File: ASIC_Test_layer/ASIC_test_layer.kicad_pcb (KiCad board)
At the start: 4 copper layers, 37.5 x 30.4 mm, 20 parts, among them J100 MOLEX-524653071, J200 MOLEX-533073071, J5 5024262030, J6 MOLEX-533073071, J7 MOLEX-524653071, P11 Header 11X2, P12 Header 11X2, P13 Header 11X2

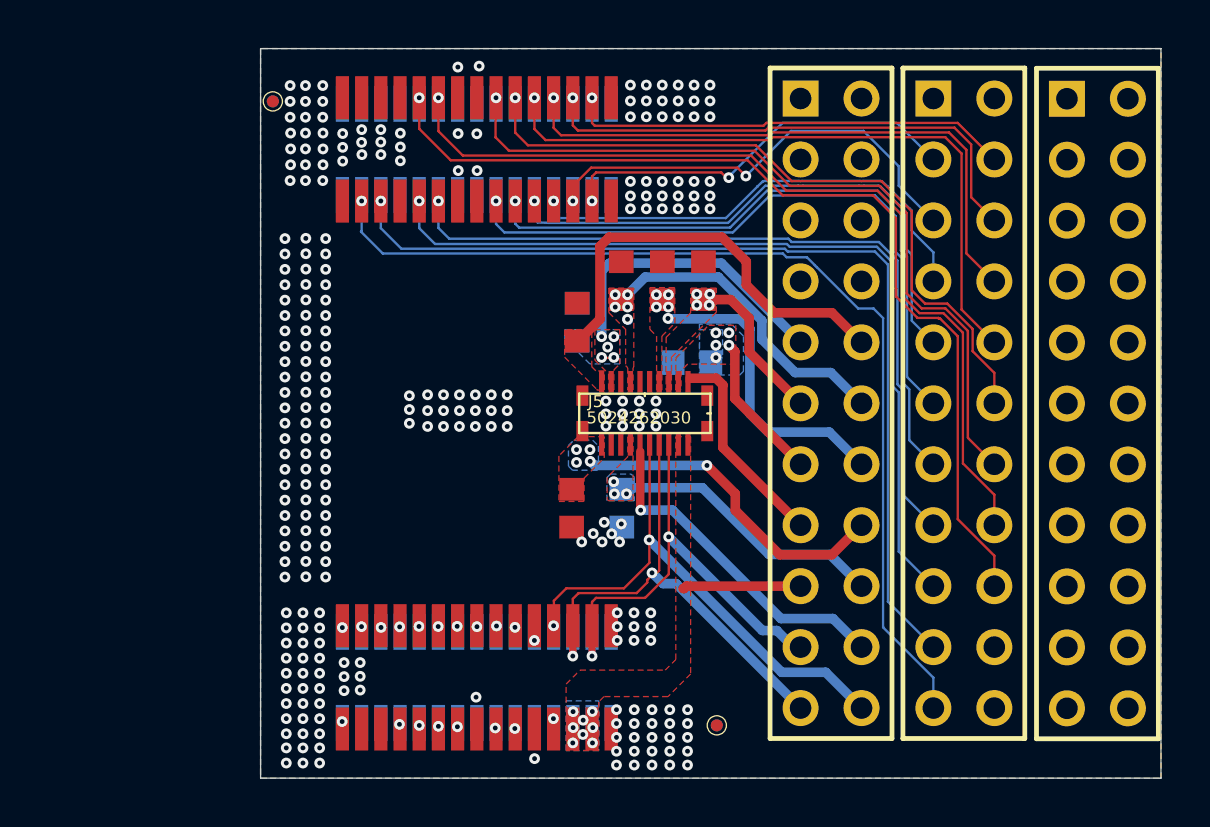
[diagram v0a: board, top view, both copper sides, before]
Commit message: fixed test layer
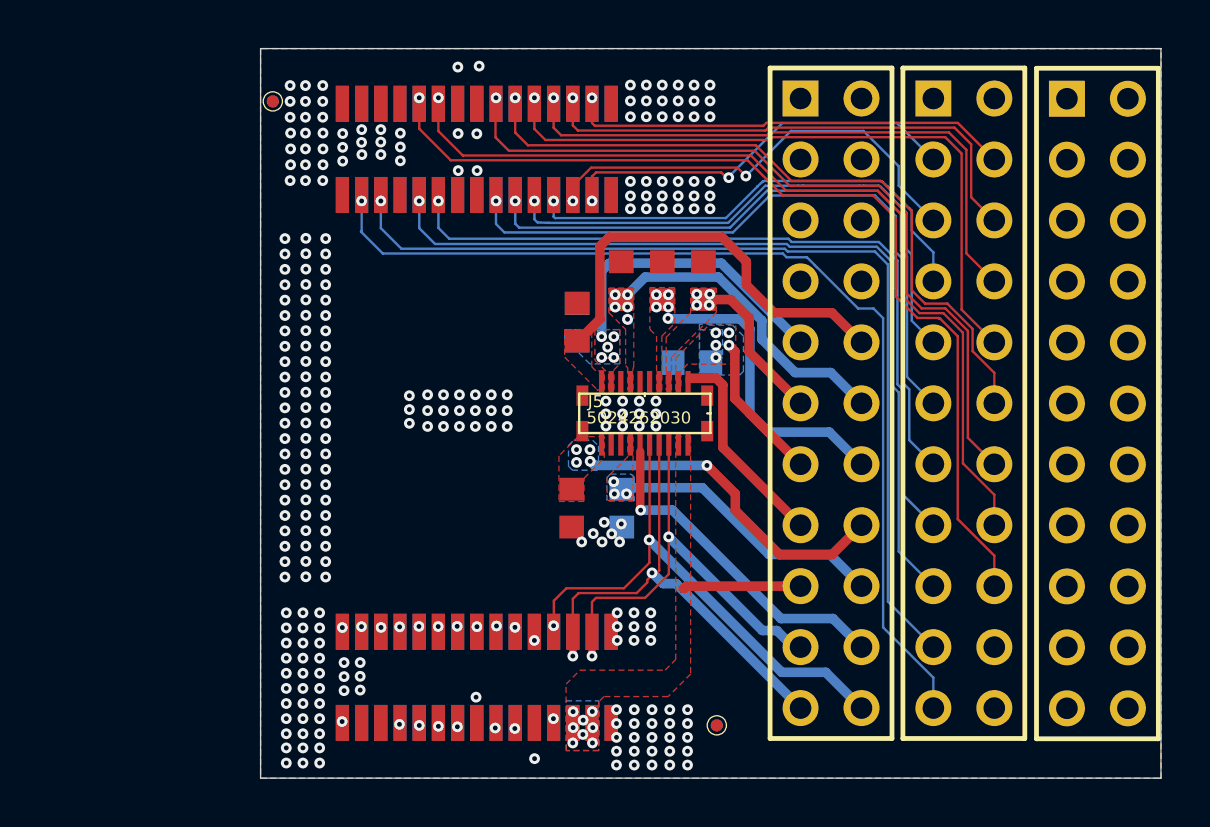
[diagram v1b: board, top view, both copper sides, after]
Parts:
- C200, C201, C202, C203, C204, C205, C206, C207: footprint Fooprints:CAPC1709X50N -> Footprints:CAPC1709X50N
- FID1, FID2, FID3, FID4: footprint Fooprints:MFID0508 -> Footprints:MFID0508
- J100, J7: footprint Fooprints:J524653071 -> FDM_footprints:J524653071_Board2Board
- J200, J6: value MOLEX-533073071 -> MOLEX-524653071; footprint Fooprints:J533073071 -> FDM_footprints:J524653071_Board2Board
- J5: footprint Fooprints:JMOLEX-0559090274V1 -> Footprints:JMOLEX-0559090274V1
- P11, P12, P13: footprint Fooprints:HDR2X11 -> Footprints:HDR2X11
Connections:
- net NetJ100_1 renamed /PB_0
- net NetJ100_10 renamed /SER_B2
- net NetJ100_11 renamed /SER_B0
- net NetJ100_19 renamed /\B_DAC_CS
- net NetJ100_2 renamed /M0_B
- net NetJ100_21 renamed /B_SER_B0
- net NetJ100_22 renamed /B_SER_B2
- net NetJ100_3 renamed /M1_B
- net NetJ100_4 renamed /PB_1
- net NetJ100_5 renamed /SER_CLK_0
- net NetJ100_6 renamed /SER_B1
- net NetJ100_7 renamed /SER_B3
- net NetJ100_8 renamed /SCLK
- net NetJ100_9 renamed /OSC_CLK
- net NetJ5_10 renamed /\DAC_CS
- net NetJ5_6 renamed /DAC_SDI
- net NetJ5_8 renamed /DAC_SCK
- net NetJ6_10 renamed /B_MODE_0
- net NetJ6_11 renamed /\B_SPI_CS
- net NetJ6_17 renamed /SPI_CLK
- net NetJ6_18 renamed /SPI_DATA
- net NetJ6_2 renamed /B_MODE_1
- net NetJ6_20 renamed /\SPI_CS
- net NetJ6_21 renamed /MODE_0
- net NetJ6_24 renamed /SER_CLK_1
- net NetJ6_25 renamed /SER_B6
- net NetJ6_26 renamed /SER_B4
- net NetJ6_27 renamed /SER_B5
- net NetJ6_28 renamed /SER_B7
- net NetJ6_29 renamed /MODE_1
- net NetJ6_3 renamed /B_SER_B7
- net NetJ6_4 renamed /B_SER_B5
- net NetJ6_5 renamed /B_SER_B4
- net NetJ6_6 renamed /B_SER_B6
- net NetJ6_7 renamed /B_SER_CLK_1
- J100 pad 20: (no net) -> unconnected-(J100-Pad20)
- J100 pad 23: (no net) -> unconnected-(J100-Pad23)
- J100 pad 24: NetJ100_24 -> /B_SER_B3
- J100 pad 25: NetJ100_25 -> /B_SER_B1
- J100 pad 26: NetJ100_26 -> /B_SER_CLK_0
- J100 pad 27: NetJ100_27 -> /B_PB_1
- J100 pad 28: (no net) -> unconnected-(J100-Pad28)
- J100 pad 29: (no net) -> unconnected-(J100-Pad29)
- J100 pad 30: NetJ100_30 -> /B_PB_0
- J200 pad 16: NetJ100_30 -> /B_PB_0
- J200 pad 17: (no net) -> unconnected-(J200-Pad17)
- J200 pad 18: (no net) -> unconnected-(J200-Pad18)
- J200 pad 19: NetJ100_27 -> /B_PB_1
- J200 pad 20: NetJ100_26 -> /B_SER_CLK_0
- J200 pad 21: NetJ100_25 -> /B_SER_B1
- J200 pad 22: NetJ100_24 -> /B_SER_B3
- J200 pad 23: (no net) -> unconnected-(J200-Pad23)
- J200 pad 26: (no net) -> unconnected-(J200-Pad26)
- J6 pad 12: (no net) -> unconnected-(J6-Pad12)
- J6 pad 13: (no net) -> unconnected-(J6-Pad13)
- J6 pad 14: (no net) -> unconnected-(J6-Pad14)
- J7 pad 2: (no net) -> unconnected-(J7-Pad2)
- J7 pad 3: (no net) -> unconnected-(J7-Pad3)
- J7 pad 4: (no net) -> unconnected-(J7-Pad4)
- P11 pad 3: (no net) -> unconnected-(P11-Pad3)
- P11 pad 4: (no net) -> unconnected-(P11-Pad4)
- P11 pad 5: (no net) -> unconnected-(P11-Pad5)
- P11 pad 6: (no net) -> unconnected-(P11-Pad6)
- P11 pad 7: (no net) -> unconnected-(P11-Pad7)
- P11 pad 8: (no net) -> unconnected-(P11-Pad8)
- P12 pad 20: (no net) -> unconnected-(P12-Pad20)
- P12 pad 22: (no net) -> unconnected-(P12-Pad22)
- P13 pad 10: NetJ100_25 -> unconnected-(P13-Pad10)
- P13 pad 12: NetJ100_24 -> unconnected-(P13-Pad12)
- P13 pad 14: (no net) -> unconnected-(P13-Pad14)
- P13 pad 4: NetJ100_30 -> unconnected-(P13-Pad4)
- P13 pad 6: NetJ100_27 -> unconnected-(P13-Pad6)
- P13 pad 8: NetJ100_26 -> unconnected-(P13-Pad8)

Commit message: Test Commint
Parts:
- added IC1: DS90UB914ATRHSJQ1, Samacsys:QFN50P700X700X80-49N, F.Cu at (125.0, 98.0)
- added U1: DS90UB913ATRTVTQ1, Samacsys:QFN50P500X500X80-33N, F.Cu at (124.0, 106.4)
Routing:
- net (no net): track 0.00 -> 219.3 mm, vias 0 -> 5
- net NetJ100_30: track 50.9 -> 0.00 mm, vias 1 -> 0
- net NetJ100_27: track 47.2 -> 0.00 mm, vias 1 -> 0
- net NetJ100_26: track 43.4 -> 0.00 mm, vias 1 -> 0
- net NetJ100_25: track 41.0 -> 0.00 mm, vias 1 -> 0
- net NetJ100_24: track 36.9 -> 0.00 mm, vias 1 -> 0
